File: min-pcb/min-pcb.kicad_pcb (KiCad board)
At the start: 2 copper layers, 38 x 25 mm, 6 parts, among them J1 Conn_Pi, J2 Conn_DCDC, J3 Conn_Ext_Btn, SW1 SW_Push, U1 74HCT74

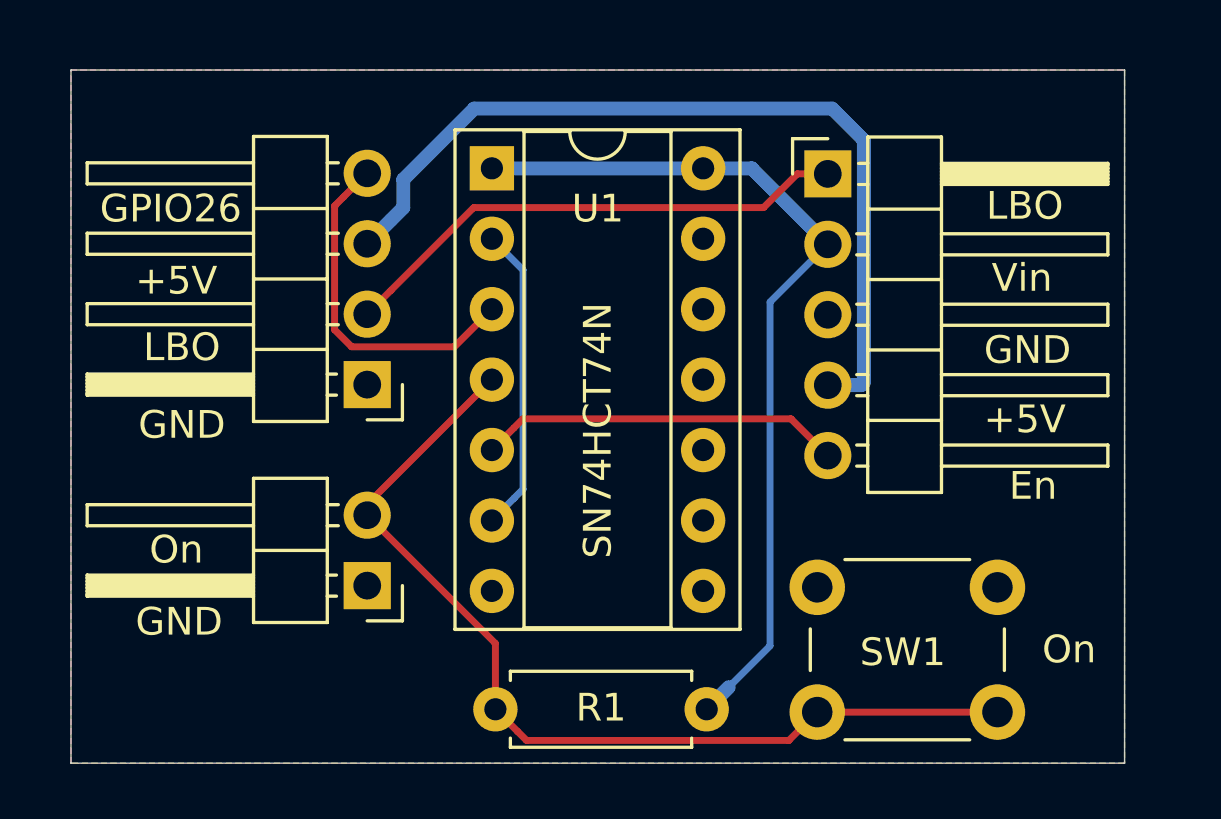
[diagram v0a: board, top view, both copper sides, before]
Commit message: optimzed traces
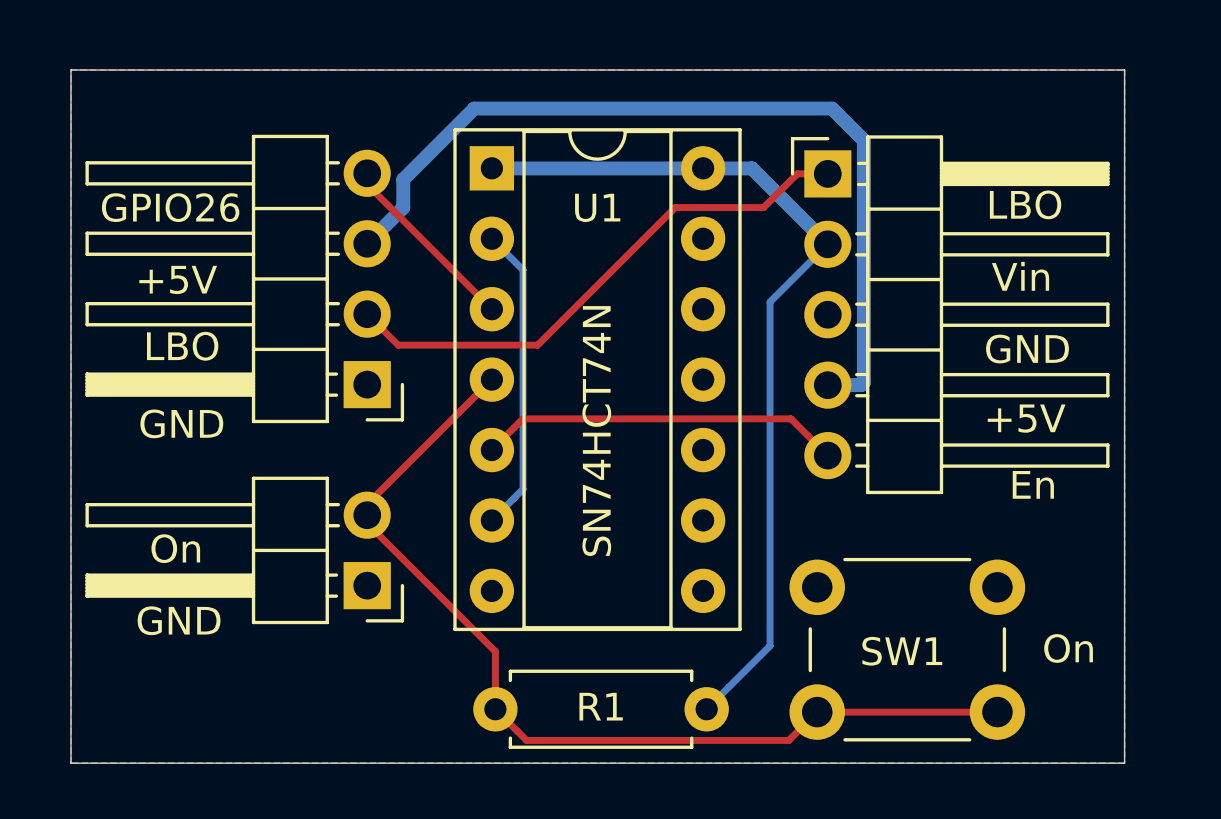
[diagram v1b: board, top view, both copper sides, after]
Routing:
- net /GPIO26: track 12.6 -> 6.76 mm
- net /LBO: track 18.7 -> 19.6 mm
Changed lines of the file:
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@@
     (thickness 1.6)
     (drawings 17)
-    (tracks 44)
+    (tracks 42)
     (zones 0)
     (modules 6)
@@
   (gr_line (start 66 17) (end 66 42) (layer Edge.Cuts) (width 0.05))
   (gr_line (start 28 17) (end 66 17) (layer Edge.Cuts) (width 0.05))
-  (segment (start 39.534199 24.956401) (end 38.6842 25.8064) (width 0.25) (layer F.Cu) (net 2))
-  (segment (start 42.529201 21.961399) (end 39.534199 24.956401) (width 0.25) (layer F.Cu) (net 2))
-  (segment (start 52.980801 21.961399) (end 42.529201 21.961399) (width 0.25) (layer F.Cu) (net 2))
+  (segment (start 39.8018 26.924) (end 38.6842 25.8064) (width 0.25) (layer F.Cu) (net 2))
   (segment (start 54.1958 20.7464) (end 52.980801 21.961399) (width 0.25) (layer F.Cu) (net 2))
+  (segment (start 44.831 26.924) (end 39.8018 26.924) (width 0.25) (layer F.Cu) (net 2))
   (segment (start 55.2958 20.7464) (end 54.1958 20.7464) (width 0.25) (layer F.Cu) (net 2))
+  (segment (start 52.980801 21.961399) (end 49.793601 21.961399) (width 0.25) (layer F.Cu) (net 2))
+  (segment (start 49.793601 21.961399) (end 44.831 26.924) (width 0.25) (layer F.Cu) (net 2))
   (segment (start 56.595801 19.536399) (end 55.449002 18.3896) (width 0.5) (layer B.Cu) (net 3))
   (segment (start 56.595801 28.26848) (end 56.595801 19.536399) (width 0.5) (layer B.Cu) (net 3))
@@
   (segment (start 42.545 18.3896) (end 39.984201 20.950399) (width 0.5) (layer B.Cu) (net 3))
   (segment (start 55.449002 18.3896) (end 42.545 18.3896) (width 0.5) (layer B.Cu) (net 3))
-  (segment (start 37.834201 21.576399) (end 38.6842 20.7264) (width 0.25) (layer F.Cu) (net 4))
-  (segment (start 37.509199 21.901401) (end 37.834201 21.576399) (width 0.25) (layer F.Cu) (net 4))
-  (segment (start 37.509199 26.370401) (end 37.509199 21.901401) (width 0.25) (layer F.Cu) (net 4))
-  (segment (start 38.120199 26.981401) (end 37.509199 26.370401) (width 0.25) (layer F.Cu) (net 4))
-  (segment (start 41.824999 26.981401) (end 38.120199 26.981401) (width 0.25) (layer F.Cu) (net 4))
-  (segment (start 43.18 25.6264) (end 41.824999 26.981401) (width 0.25) (layer F.Cu) (net 4))
+  (segment (start 38.6842 21.1306) (end 38.6842 20.7264) (width 0.25) (layer F.Cu) (net 4))
+  (segment (start 43.18 25.6264) (end 38.6842 21.1306) (width 0.25) (layer F.Cu) (net 4))
   (segment (start 43.979999 29.906401) (end 43.18 30.7064) (width 0.25) (layer F.Cu) (net 5))
   (segment (start 44.305001 29.581399) (end 43.979999 29.906401) (width 0.25) (layer F.Cu) (net 5))
@@
   (segment (start 55.2958 23.2864) (end 52.5558 20.5464) (width 0.5) (layer B.Cu) (net 6))
   (segment (start 50.8 20.5464) (end 43.18 20.5464) (width 0.5) (layer B.Cu) (net 6))
-  (segment (start 51.726999 39.255801) (end 50.927 40.0558) (width 0.5) (layer B.Cu) (net 6))
+  (segment (start 51.726999 39.255801) (end 50.927 40.0558) (width 0.25) (layer B.Cu) (net 6))
   (segment (start 53.213 37.7698) (end 51.726999 39.255801) (width 0.25) (layer B.Cu) (net 6))
   (segment (start 55.2958 23.2864) (end 53.213 25.3692) (width 0.25) (layer B.Cu) (net 6))
@@
   (segment (start 53.891399 41.180801) (end 44.432001 41.180801) (width 0.25) (layer F.Cu) (net 7))
   (segment (start 54.9148 40.1574) (end 53.891399 41.180801) (width 0.25) (layer F.Cu) (net 7))
-  (segment (start 43.307 37.6792) (end 38.6842 33.0564) (width 0.25) (layer F.Cu) (net 7))
-  (segment (start 43.307 40.0558) (end 43.307 37.6792) (width 0.25) (layer F.Cu) (net 7))
+  (segment (start 38.6842 33.3502) (end 38.6842 33.0564) (width 0.25) (layer F.Cu) (net 7))
+  (segment (start 43.307 40.0558) (end 43.307 37.973) (width 0.25) (layer F.Cu) (net 7))
+  (segment (start 43.307 37.973) (end 38.6842 33.3502) (width 0.25) (layer F.Cu) (net 7))
   (segment (start 43.979999 32.446401) (end 43.18 33.2464) (width 0.25) (layer B.Cu) (net 9))
   (segment (start 44.305001 32.121399) (end 43.979999 32.446401) (width 0.25) (layer B.Cu) (net 9))

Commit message: rearranged pins on connectors
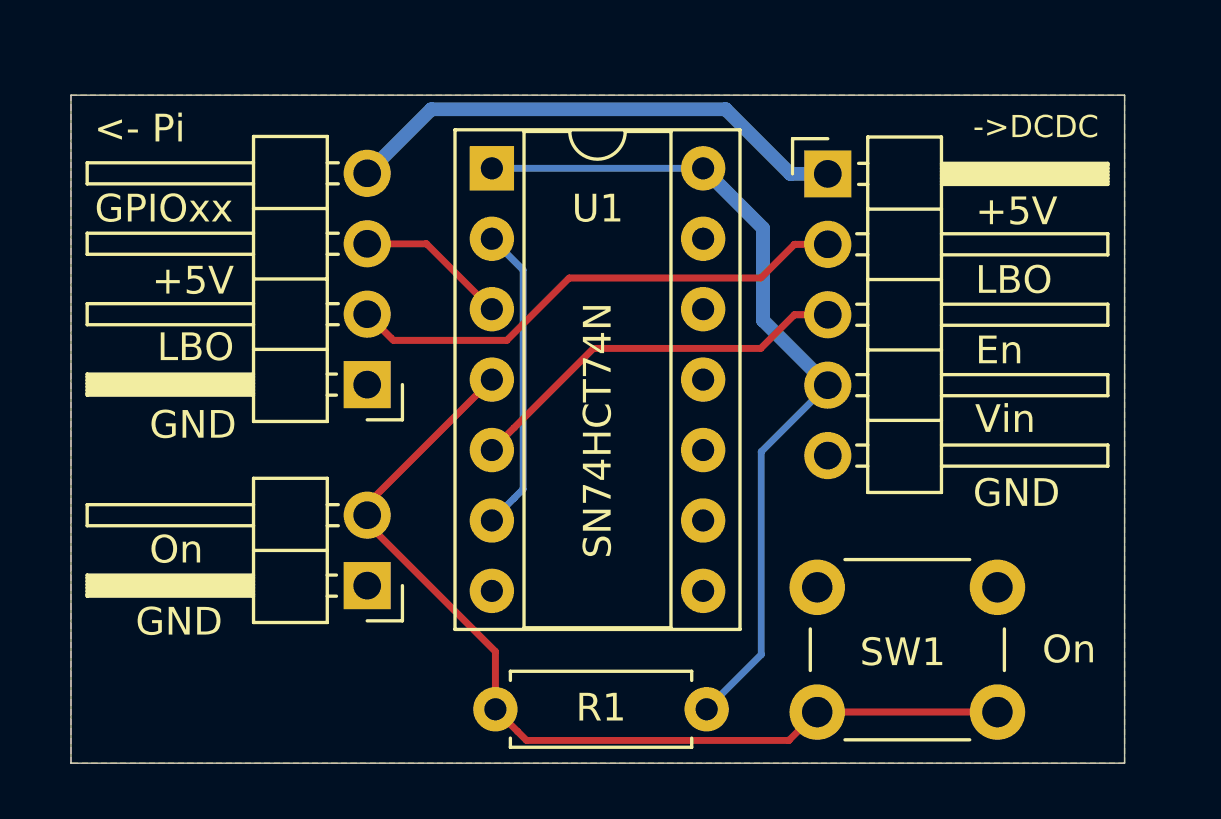
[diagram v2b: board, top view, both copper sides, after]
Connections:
- J1 pad 3: /+5V -> /GPIO26
- J1 pad 4: /GPIO26 -> /+5V
- J2 pad 1: /LBO -> /+5V
- J2 pad 2: /Vin -> /LBO
- J2 pad 3: GND -> /En
- J2 pad 4: /+5V -> /Vin
- J2 pad 5: /En -> GND
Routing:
- net /+5V: track 31.1 -> 18.5 mm
- net /GPIO26: track 6.76 -> 5.47 mm
- net /LBO: track 19.6 -> 18.4 mm
- net /Vin: track 31.8 -> 30.8 mm
- net /En: track 13.1 -> 14.1 mm
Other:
- board size 38 x 25 mm -> 38 x 24.1 mm
- board text added: "->DCDC"
- board text added: "<- Pi"
- board text added: "GPIOxx"
- board text added: "Rev 1"
- board text added: "https://github.com/bablokb/pcb-pi-batman"
- board text removed: "GPIO26"

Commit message: Rev2: added power to external connector, added mounting-holes
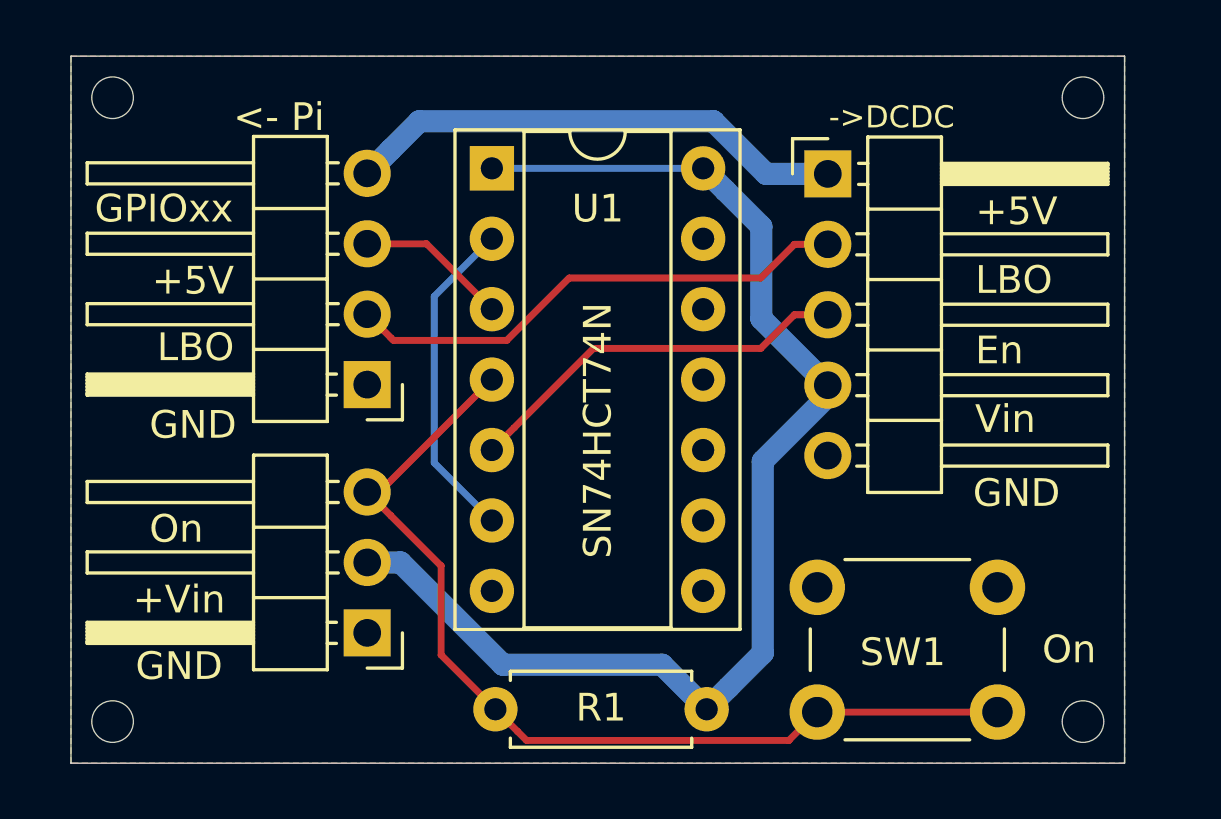
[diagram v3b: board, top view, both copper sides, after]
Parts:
- added REF**: MountingHole_1.5mm, user:MountingHole_1.5mm, F.Cu at (29.5, 40.5)
- added REF**: MountingHole_1.5mm, user:MountingHole_1.5mm, F.Cu at (64.5, 40.5)
- added REF**: MountingHole_1.5mm, user:MountingHole_1.5mm, F.Cu at (64.5, 18.0)
- added REF**: MountingHole_1.5mm, user:MountingHole_1.5mm, F.Cu at (29.5, 18.0)
- J3: value Conn_Ext_Btn -> Conn_Ext; footprint Connector_PinHeader_2.54mm:PinHeader_1x02_P2.54mm_Horizontal -> Connector_PinHeader_2.54mm:PinHeader_1x03_P2.54mm_Horizontal
- moved J3 1.70 mm to (38.7, 37.3)
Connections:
- net /GPIO26 renamed /GPIOxx
- J3 pad 2: Net-(J3-Pad2) -> /Vin
- R1 pad 1: Net-(J3-Pad2) -> Net-(J3-Pad3)
- SW1 pad 2: Net-(J3-Pad2) -> Net-(J3-Pad3)
- U1 pad 4: Net-(J3-Pad2) -> Net-(J3-Pad3)
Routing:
- net Net-(J3-Pad3): track 0.00 -> 35.1 mm
- net Net-(J3-Pad2): track 34.7 -> 0.00 mm
- net /Vin: track 30.8 -> 45.2 mm
- net Net-(U1-Pad2): track 11.1 -> 11.9 mm
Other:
- board size 38 x 24.1 mm -> 38 x 25.5 mm
- net class Power: trace_width 0.5 -> 0.8
- board text added: "+Vin"
- board text added: "Rev 2"
- board text removed: "Rev 1"

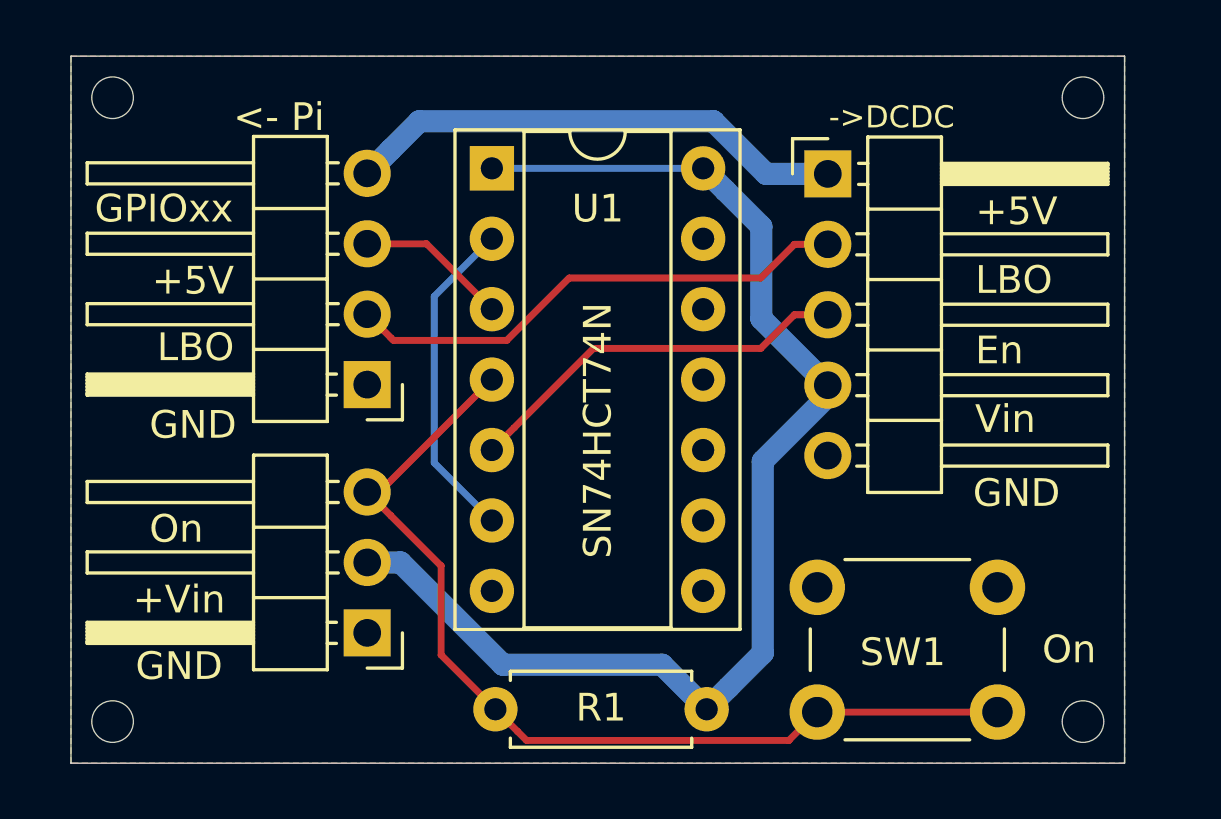
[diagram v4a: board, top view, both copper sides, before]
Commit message: minor adjustment of connector positions to have some space for terminal-blocks
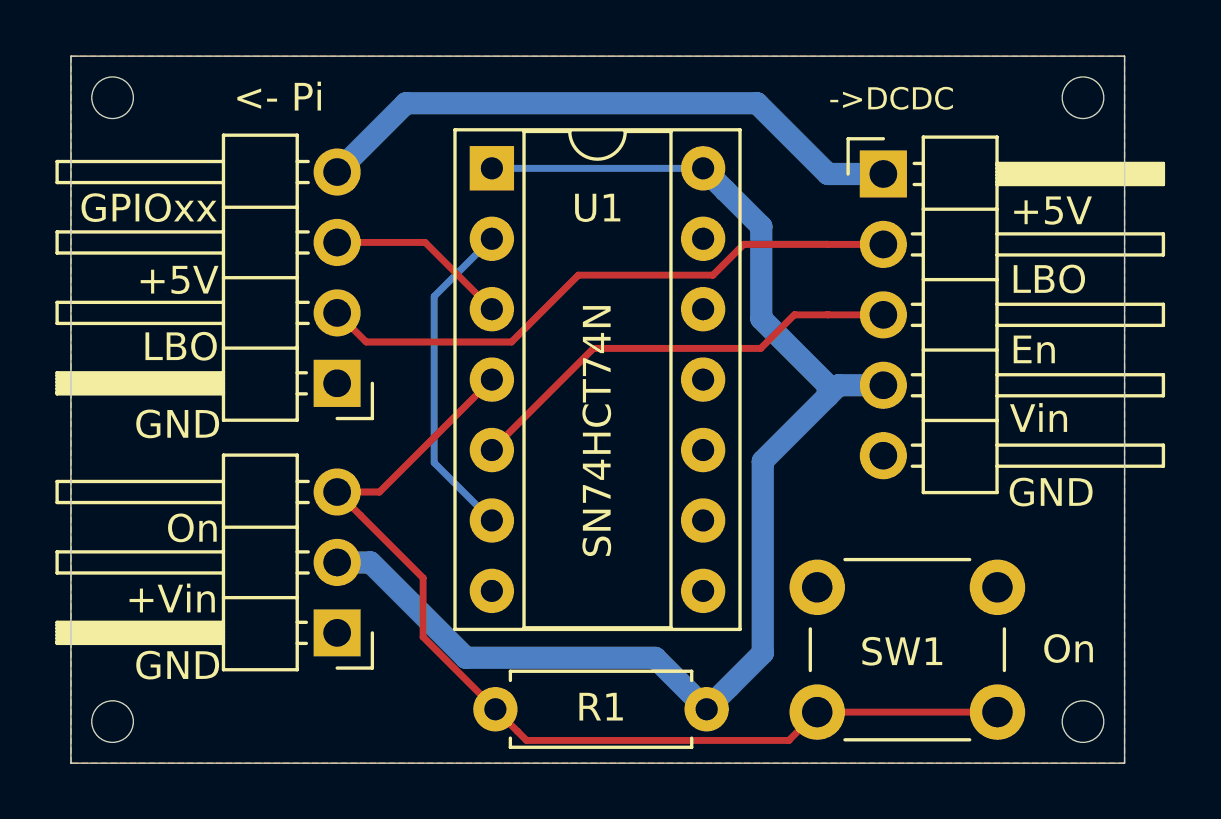
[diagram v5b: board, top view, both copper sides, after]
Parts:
- moved J2 2.00 mm to (57.3, 20.8)
- moved J1 1.09 mm to (37.6, 28.3)
- moved J3 1.08 mm to (37.6, 37.3)
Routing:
- net /+5V: track 18.2 -> 21.8 mm
- net /Vin: track 45.2 -> 48.5 mm
- net /LBO: track 18.4 -> 21.6 mm
- net /En: track 14.1 -> 16.1 mm
- net Net-(J3-Pad3): track 35.1 -> 36.5 mm
- net /GPIOxx: track 5.47 -> 6.58 mm

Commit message: added textfield for JLC production-number
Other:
- board text added: "JLCJLCJLCJLC"
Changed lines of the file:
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@@
   (general
     (thickness 1.6)
-    (drawings 22)
+    (drawings 23)
     (tracks 50)
     (zones 0)
@@
     )
   )
+  (gr_text JLCJLCJLCJLC (at 48.65 30.05 90) (layer F.SilkS)
+    (effects (font (size 1 1) (thickness 0.15)))
+  )
   (gr_text +Vin (at 31.635715 36.1) (layer F.SilkS)
     (effects (font (size 1 1) (thickness 0.15)))
@@
     (effects (font (size 1 1) (thickness 0.15)))
   )
-  (gr_text SN74HCT74N (at 47 30 90) (layer F.SilkS)
-    (effects (font (size 1 1) (thickness 0.15)))
-  )
+  (gr_text SN74HCT74N (at 45.75 30.3 90) (layer F.SilkS)
+    (effects (font (size 1 1) (thickness 0.15)))
+  )
